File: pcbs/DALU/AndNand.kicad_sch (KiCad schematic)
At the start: 6 parts, among them U501 74HC00, U502 74HC00, U503 74HC14, U504 74HC14, U505 74HC245, U506 74HC245

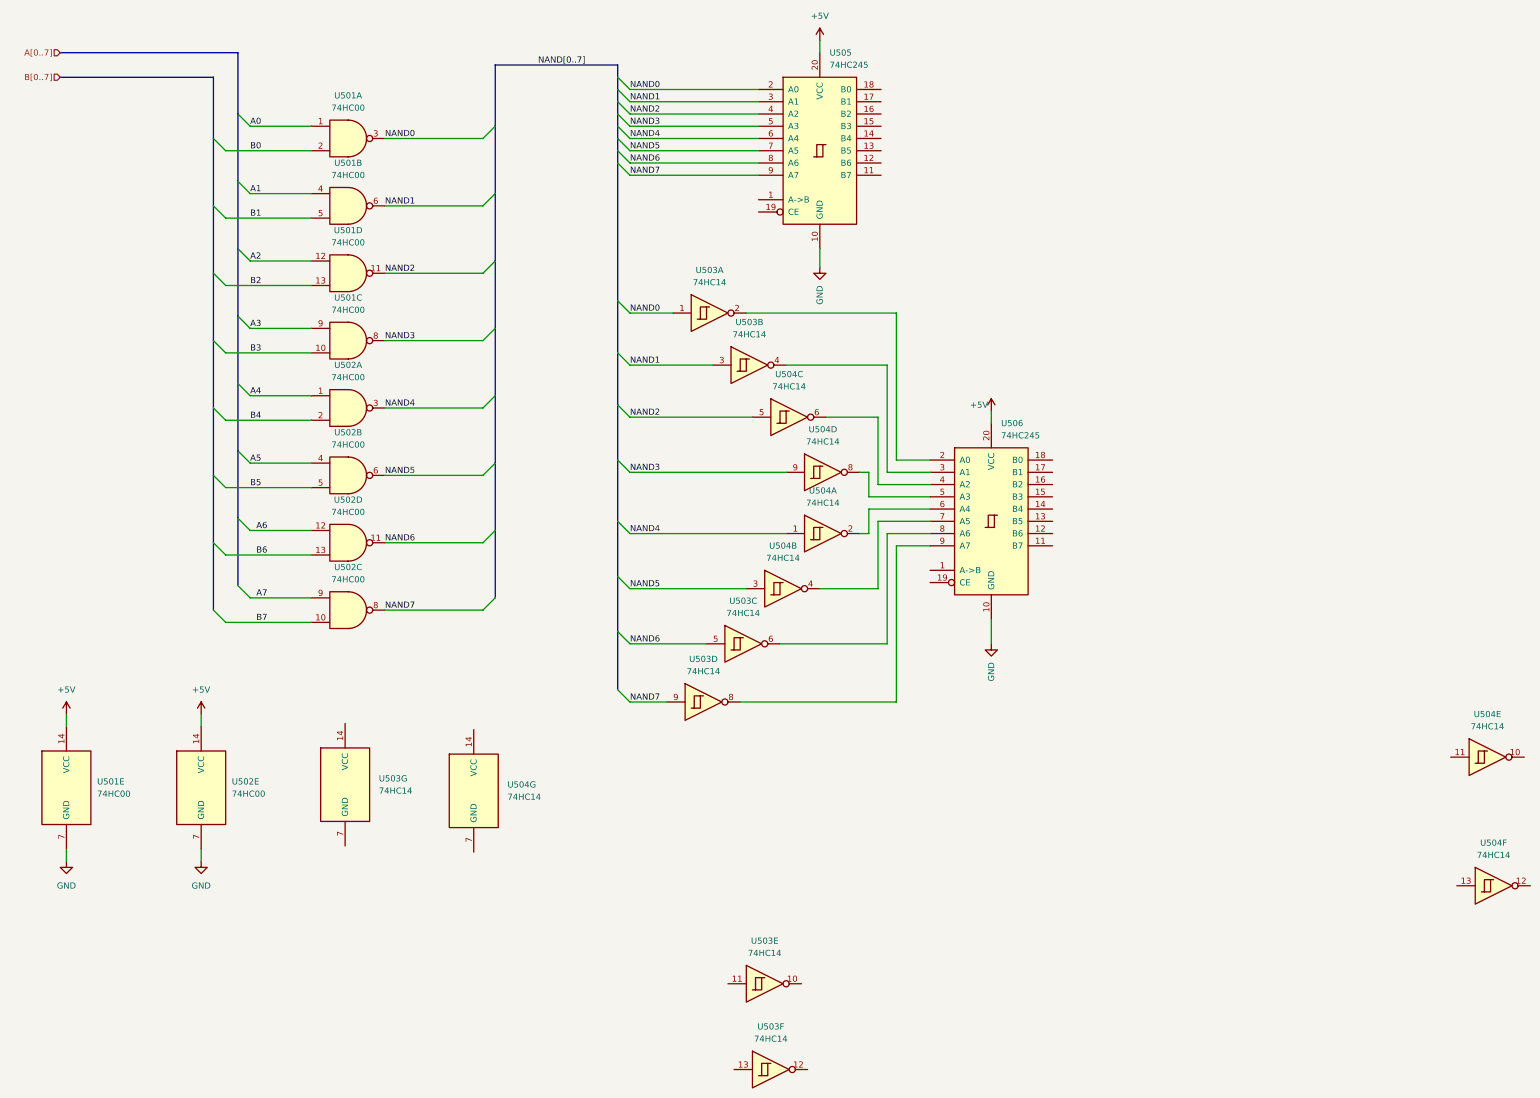
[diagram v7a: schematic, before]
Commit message: Rerouting
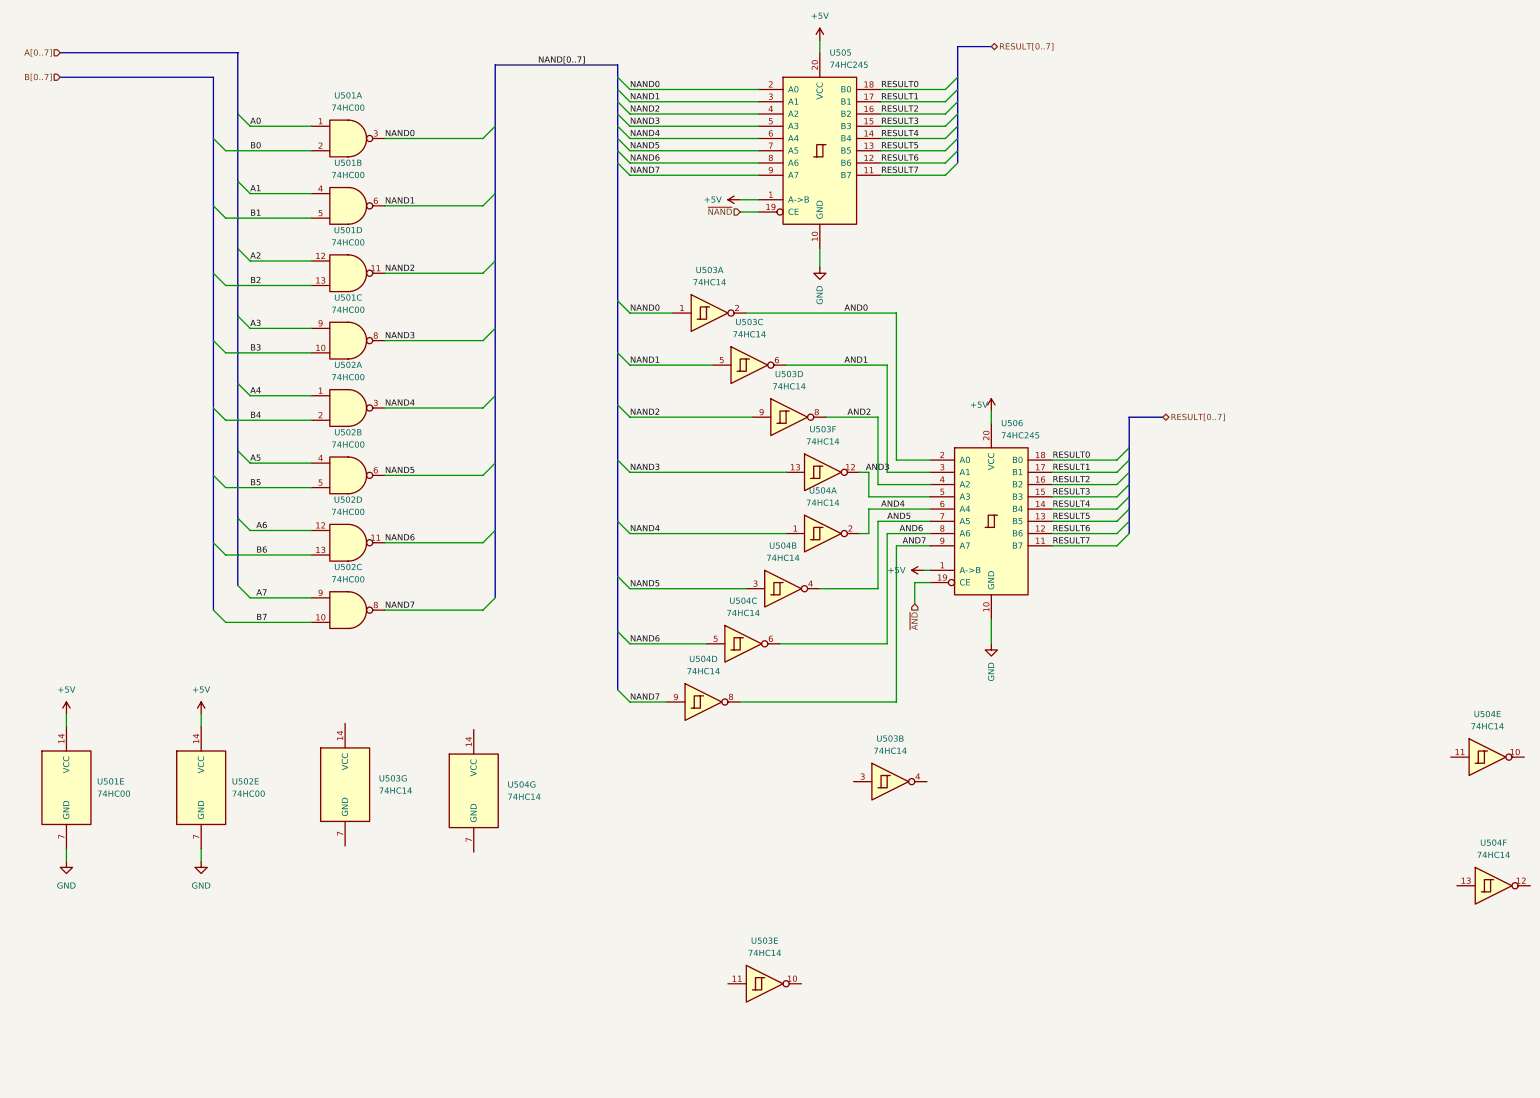
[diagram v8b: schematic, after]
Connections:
- net +5V: now also U505.1 (A->B), U506.1 (A->B)
- net NAND1: now also U503.5; no longer U503.3
- net NAND2: now also U503.9; no longer U504.5
- net NAND3: now also U503.13; no longer U504.9
- net NAND6: now also U504.5; no longer U503.5
- net NAND7: now also U504.9; no longer U503.9
- net AND0: now reaches U503.2, U506.2 (A0)
- net at U503.4: no longer U506.3 (A1)
- net AND2: now reaches U506.4 (A2)
- net AND2: now also U503.8; no longer U504.6
- net AND5: now reaches U504.4, U506.7 (A5)
- net AND4: now reaches U504.2, U506.6 (A4)
- net AND1: now reaches U503.6
- net AND1: now also U506.3 (A1); no longer U506.8 (A6)
- net AND7: now reaches U506.9 (A7)
- net AND7: now also U504.8; no longer U503.8
- net AND3: now reaches U506.5 (A3)
- net AND3: now also U503.12; no longer U504.8
- net RESULT7: now reaches U505.11 (B7)
- net RESULT7: now also U506.11 (B7)
- net RESULT6: now reaches U505.12 (B6)
- net RESULT6: now also U506.12 (B6)
- net RESULT5: now reaches U505.13 (B5)
- net RESULT5: now also U506.13 (B5)
- net RESULT4: now reaches U505.14 (B4)
- net RESULT4: now also U506.14 (B4)
- net RESULT3: now reaches U505.15 (B3)
- net RESULT3: now also U506.15 (B3)
- net RESULT2: now reaches U505.16 (B2)
- net RESULT2: now also U506.16 (B2)
- net RESULT1: now reaches U505.17 (B1)
- net RESULT1: now also U506.17 (B1)
- net RESULT0: now reaches U505.18 (B0)
- net RESULT0: now also U506.18 (B0)
- net ~{NAND}: now reaches U505.19 (CE)
- net ~{AND}: now reaches U506.19 (CE)
- new net AND6: U504.6, U506.8 (A6)
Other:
- moved on the sheet: U503B, U503C, U503D, U503F, U504C, U504D
